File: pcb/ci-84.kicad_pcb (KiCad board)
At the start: 2 copper layers, 91 x 217 mm, 113 parts, among them J1 Conn_01x02, SW1 SW_Push, SW10 XT0N, SW11 STAT, SW12 MATH, SW13 APPS, SW14 PRGM, SW15 VARS, SW16 CLEAR, SW17 X^-1, SW18 SIN, SW19 COS, SW2 Y=, SW20 TAN, SW21 ^, SW22 X^2, SW23 ,, SW24 (, SW25 ), SW26 DIVIDE, SW27 LOG, SW28 7, SW29 8, SW3 WINDOW, SW30 9, SW31 MULITPLY, SW32 IN, SW33 4, SW34 5, SW35 6, SW36 SUBTRACT, SW37 STO, SW38 1, SW39 2, SW4 ZOOM, SW40 3, SW41 ADD, SW42 ON, SW43 0, SW44 ., SW45 (-), SW46 ENTER, SW47 GRAPH, SW48 UP, SW49 RIGHT, SW5 TRACE, SW50 DOWN, SW51 LEFT, SW6 2ND, SW7 MODE, SW8 DEL, SW9 ALPHA, U1 STM32L471RGTx, U3 TPS63900, U4 TFT_320x240

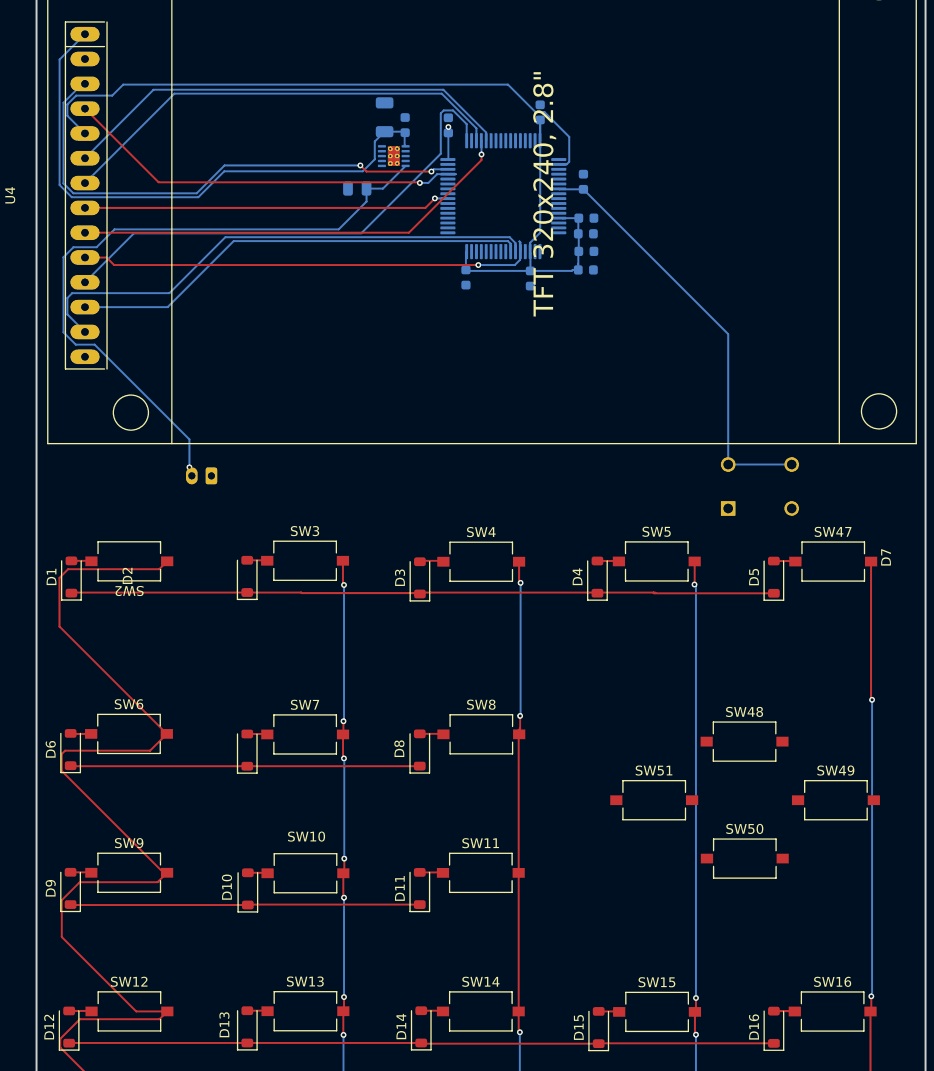
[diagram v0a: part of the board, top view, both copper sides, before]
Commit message: move arrow keys to keyboard matrix, add labels for riows
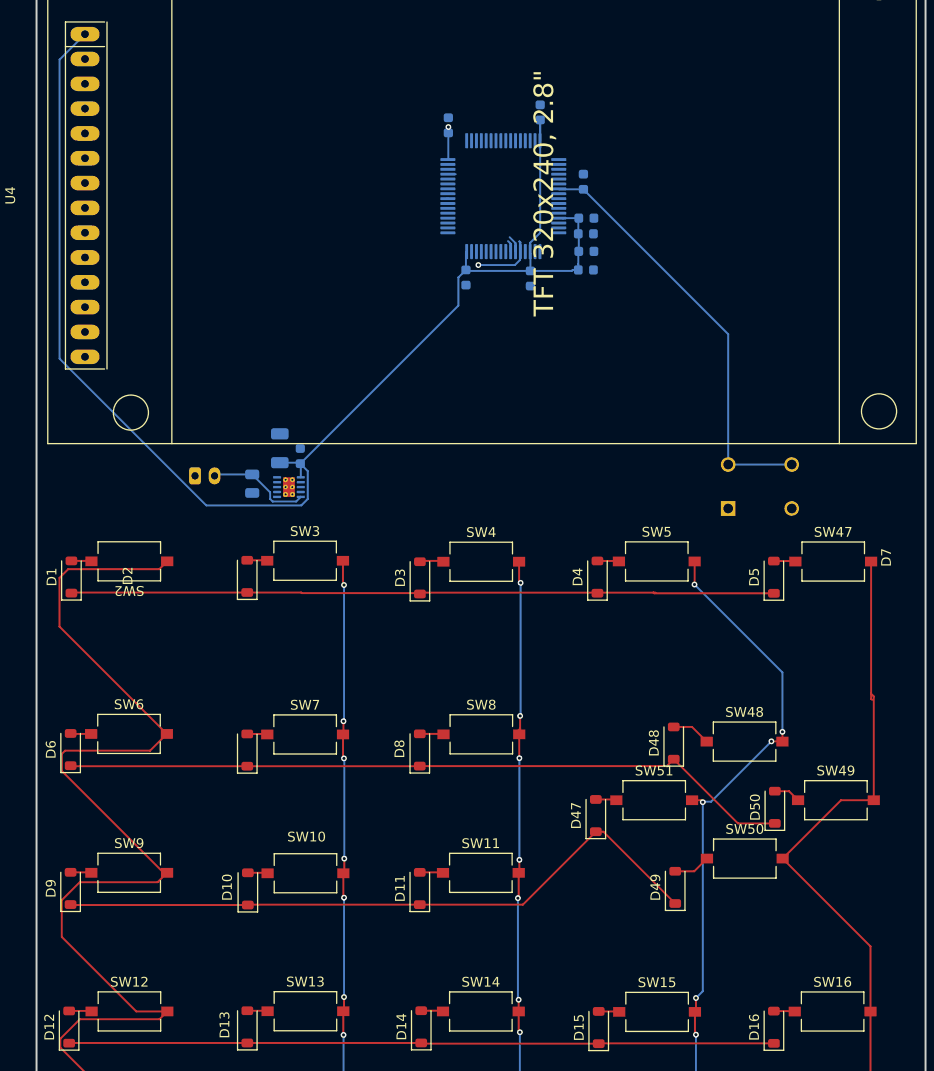
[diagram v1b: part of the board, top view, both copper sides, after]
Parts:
- added D47: D, Diode_SMD:D_SOD-123, F.Cu at (294.8, 182.7)
- added D48: D, Diode_SMD:D_SOD-123, F.Cu at (302.7, 175.2)
- added D49: D, Diode_SMD:D_SOD-123, F.Cu at (302.9, 190.0)
- added D50: D, Diode_SMD:D_SOD-123, F.Cu at (313.1, 181.8)
- moved U3 35.5 mm to (263.3, 149.1)
- moved C12 35.5 mm to (262.4, 145.1)
- moved C5 35.5 mm to (264.5, 145.9)
- moved C11 32.1 mm to (259.6, 148.7), turned to 90 degrees
- moved J1 1.68 mm to (253.7, 147.9), turned to 0 degrees
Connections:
- net Net-(D1-K) renamed /r1
- net Net-(D10-K) renamed /r3
- net Net-(D12-K) renamed /r4
- net Net-(D17-K) renamed /r5
- net Net-(D22-K) renamed /r6
- net Net-(D27-K) renamed /r7
- net Net-(D32-K) renamed /r8
- net Net-(D37-K) renamed /r9
- net Net-(D42-K) renamed /r10
- net Net-(D6-K) renamed /r2
- net Net-(SW10-Pad2) renamed /c2
- net Net-(SW11-Pad2) renamed /c3
- net Net-(SW12-Pad2) renamed /c1
- SW15 pad 2: Net-(SW15-Pad2) -> /c4
- SW16 pad 2: Net-(SW16-Pad2) -> /c5
- SW20 pad 2: Net-(SW15-Pad2) -> /c4
- SW21 pad 2: Net-(SW16-Pad2) -> /c5
- SW25 pad 2: Net-(SW15-Pad2) -> /c4
- SW26 pad 2: Net-(SW16-Pad2) -> /c5
- SW30 pad 2: Net-(SW15-Pad2) -> /c4
- SW31 pad 2: Net-(SW16-Pad2) -> /c5
- SW35 pad 2: Net-(SW15-Pad2) -> /c4
- SW36 pad 2: Net-(SW16-Pad2) -> /c5
- SW40 pad 2: Net-(SW15-Pad2) -> /c4
- SW41 pad 2: Net-(SW16-Pad2) -> /c5
- SW45 pad 2: Net-(SW15-Pad2) -> /c4
- SW46 pad 2: Net-(SW16-Pad2) -> /c5
- SW47 pad 2: Net-(SW16-Pad2) -> /c5
- SW48 pad 1: unconnected-(SW48-Pad1) -> Net-(D48-A)
- SW48 pad 2: unconnected-(SW48-Pad2) -> /c4
- SW49 pad 1: unconnected-(SW49-Pad1) -> Net-(D50-A)
- SW49 pad 2: unconnected-(SW49-Pad2) -> /c5
- SW5 pad 2: Net-(SW15-Pad2) -> /c4
- SW50 pad 1: unconnected-(SW50-Pad1) -> Net-(D49-A)
- SW50 pad 2: unconnected-(SW50-Pad2) -> /c5
- SW51 pad 1: unconnected-(SW51-Pad1) -> Net-(D47-A)
- SW51 pad 2: unconnected-(SW51-Pad2) -> /c4
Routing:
- net /c4: track 0.00 -> 152.5 mm, vias 0 -> 17
- net Net-(SW15-Pad2): track 142.9 -> 0.00 mm, vias 14 -> 0
- net /c5: track 0.00 -> 141.9 mm
- net Net-(SW16-Pad2): track 131.6 -> 0.00 mm, vias 2 -> 0
- net /IO_DC: track 61.9 -> 0.00 mm
- net +BATT: track 67.8 -> 10.6 mm, vias 1 -> 0
- net /SPI_CS: track 53.0 -> 0.66 mm, vias 2 -> 0
- net /TS_MISO: track 53.8 -> 1.72 mm
- net /TS_CS: track 51.1 -> 0.00 mm
- net /SPI3_MOSI: track 46.6 -> 0.00 mm
- net /SPI3_SCK: track 46.6 -> 0.00 mm
- net /TS_MOSI: track 47.3 -> 1.19 mm
- net /SPI_MISO: track 45.7 -> 0.03 mm, vias 1 -> 0
- net VDD: track 99.4 -> 142.1 mm
- net /SCREEN_RST: track 42.3 -> 0.81 mm, vias 1 -> 0
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
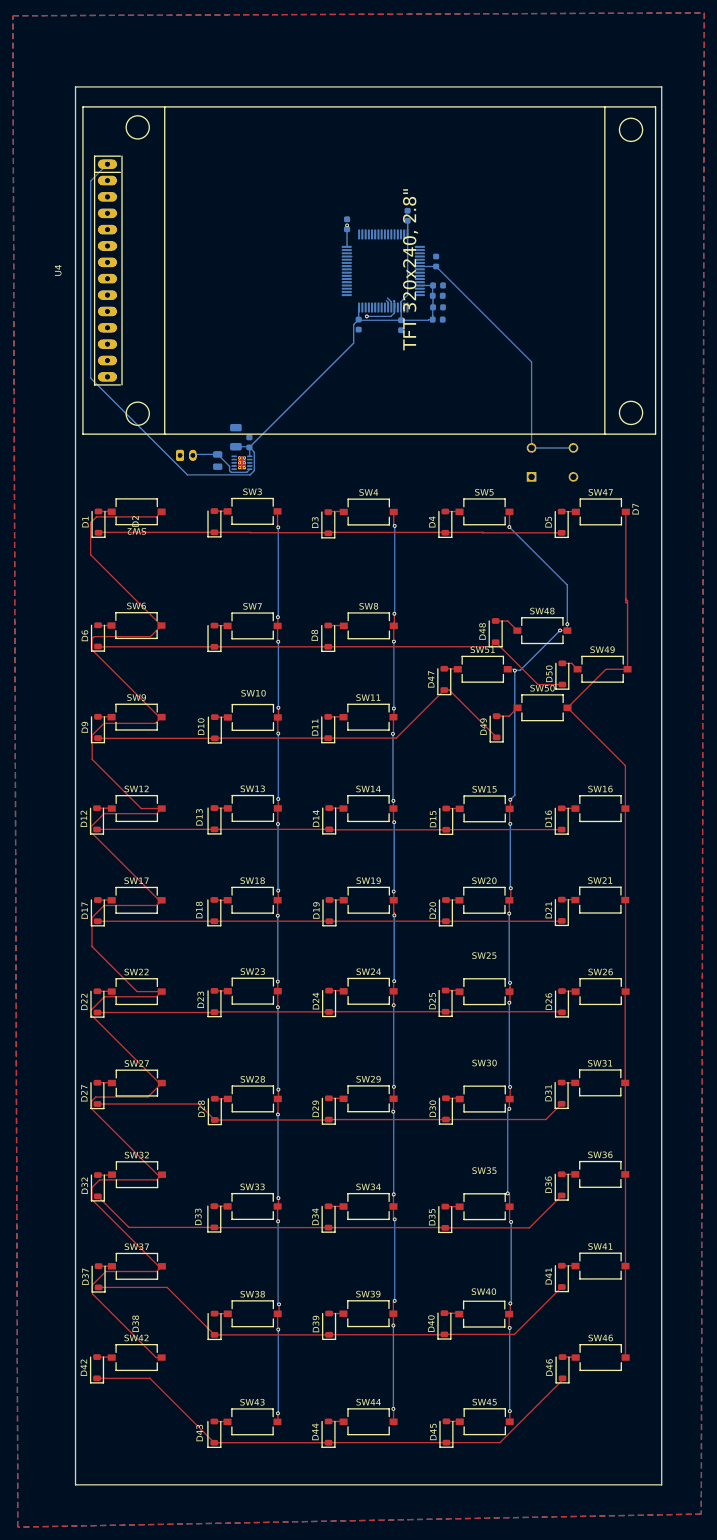
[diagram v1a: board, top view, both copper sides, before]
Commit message: finish matrix connections
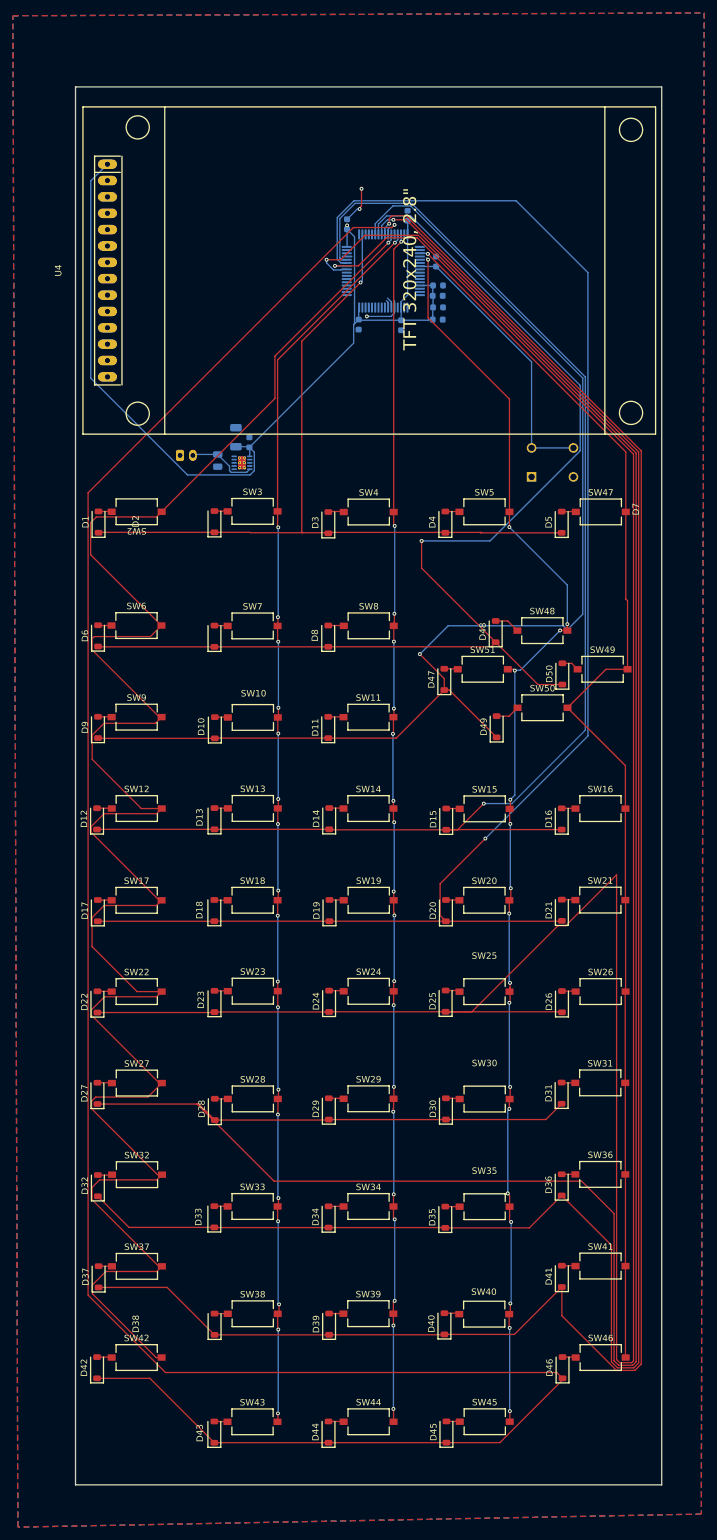
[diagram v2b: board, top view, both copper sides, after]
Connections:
- U1 pad 3: unconnected-(U1-PC14-Pad3) -> /c5
- U1 pad 4: unconnected-(U1-PC15-Pad4) -> /c4
- U1 pad 41: unconnected-(U1-PA8-Pad41) -> /r7
- U1 pad 42: unconnected-(U1-PA9-Pad42) -> /r6
- U1 pad 43: unconnected-(U1-PA10-Pad43) -> /r5
- U1 pad 44: unconnected-(U1-PA11-Pad44) -> /r4
- U1 pad 50: unconnected-(U1-PA15-Pad50) -> /r1
- U1 pad 54: unconnected-(U1-PD2-Pad54) -> /r3
- U1 pad 55: unconnected-(U1-PB3-Pad55) -> /r2
- U1 pad 56: unconnected-(U1-PB4-Pad56) -> /r8
- U1 pad 57: unconnected-(U1-PB5-Pad57) -> /r9
- U1 pad 58: unconnected-(U1-PB6-Pad58) -> /r10
- U1 pad 59: unconnected-(U1-PB7-Pad59) -> /c1
- U1 pad 61: unconnected-(U1-PB8-Pad61) -> /c2
- U1 pad 62: unconnected-(U1-PB9-Pad62) -> /c3
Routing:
- net /r6: track 72.2 -> 390.4 mm, vias 0 -> 1
- net /r7: track 74.1 -> 381.5 mm, vias 0 -> 1
- net /r10: track 80.7 -> 351.2 mm, vias 0 -> 1
- net /r8: track 76.1 -> 308.0 mm, vias 0 -> 1
- net /r9: track 78.0 -> 297.7 mm, vias 0 -> 1
- net /r5: track 72.1 -> 235.4 mm, vias 0 -> 1
- net /r4: track 72.2 -> 212.7 mm, vias 0 -> 1
- net /r3: track 68.1 -> 186.1 mm, vias 0 -> 1
- net /r2: track 75.2 -> 180.8 mm, vias 0 -> 1
- net /c1: track 262.4 -> 320.2 mm, vias 0 -> 1
- net /c5: track 141.9 -> 195.3 mm, vias 0 -> 1
- net /c2: track 142.2 -> 192.9 mm, vias 18 -> 19
- net /r1: track 72.2 -> 122.6 mm, vias 0 -> 1
- net /c4: track 152.5 -> 197.3 mm, vias 17 -> 18
- net /c3: track 142.3 -> 185.9 mm, vias 18 -> 19
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
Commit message: finish wiring everthing
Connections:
- U1 pad 2: /IO_DC -> unconnected-(U1-PC13-Pad2)
- U1 pad 21: /TS_CK -> unconnected-(U1-PA5-Pad21)
- U1 pad 22: /TS_MISO -> unconnected-(U1-PA6-Pad22)
- U1 pad 23: /TS_MOSI -> unconnected-(U1-PA7-Pad23)
- U1 pad 33: unconnected-(U1-PB12-Pad33) -> /TS_MISO
- U1 pad 34: unconnected-(U1-PB13-Pad34) -> /TS_MOSI
- U1 pad 35: unconnected-(U1-PB14-Pad35) -> /TS_CS
- U1 pad 36: unconnected-(U1-PB15-Pad36) -> /TS_CK
- U1 pad 37: unconnected-(U1-PC6-Pad37) -> /IO_LED
- U1 pad 38: unconnected-(U1-PC7-Pad38) -> /SPI3_SCK
- U1 pad 39: unconnected-(U1-PC8-Pad39) -> /SCREEN_RST
- U1 pad 40: /IO_LED -> /SPI_CS
- U1 pad 45: /SCREEN_RST -> unconnected-(U1-PA12-Pad45)
- U1 pad 46: /SPI_CS -> unconnected-(U1-PA13-Pad46)
- U1 pad 49: /TS_CS -> /IO_DC
- U1 pad 51: /SPI3_SCK -> unconnected-(U1-PC10-Pad51)
- U1 pad 52: /SPI_MISO -> /SPI3_MOSI
- U1 pad 53: /SPI3_MOSI -> /SPI_MISO
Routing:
- net /SPI_MISO: track 0.03 -> 65.7 mm, vias 0 -> 1
- net /SPI3_MOSI: track 0.00 -> 50.9 mm, vias 0 -> 1
- net /IO_DC: track 0.00 -> 42.3 mm, vias 0 -> 1
- net /SPI_CS: track 0.66 -> 42.7 mm
- net /SCREEN_RST: track 0.81 -> 41.2 mm
- net /TS_CS: track 0.00 -> 39.7 mm
- net /TS_MISO: track 1.72 -> 41.3 mm
- net /TS_MOSI: track 1.19 -> 40.5 mm
- net /SPI3_SCK: track 0.00 -> 38.3 mm
- net /IO_LED: track 0.03 -> 38.0 mm
- net /TS_CK: track 7.47 -> 38.8 mm, vias 1 -> 0
- net GND: track 5.88 -> 24.4 mm, vias 2 -> 5
- net /c4: track 197.3 -> 198.4 mm
- net unconnected-(U1-PA12-Pad45): track 0.00 -> 0.81 mm
- net VDD: vias 1 -> 0

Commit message: sheets for schematic
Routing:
- net GND: track 24.4 -> 37.0 mm, vias 5 -> 8
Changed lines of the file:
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@@
 			(outputformat 1)
 			(mirror no)
-			(drillshape 1)
+			(drillshape 0)
 			(scaleselection 1)
-			(outputdirectory "")
+			(outputdirectory "../../../Downloads/")
 		)
 	)
@@
 	)
 	(segment
+		(start 255.85 149.75)
+		(end 254.275 151.325)
+		(width 0.2)
+		(layer "F.Cu")
+		(net 2)
+	)
+	(segment
 		(start 281.6 109.65)
 		(end 281.6 109.45)
@@
 	)
 	(segment
+		(start 281.45 123.65)
+		(end 278.625 126.475)
+		(width 0.2)
+		(layer "F.Cu")
+		(net 2)
+	)
+	(segment
 		(start 281.673527 115.35)
 		(end 283.35 115.35)
@@
 	)
 	(segment
+		(start 254.275 151.325)
+		(end 253.25 151.325)
+		(width 0.2)
+		(layer "F.Cu")
+		(net 2)
+	)
+	(segment
 		(start 281.6 109.45)
 		(end 281.9 109.15)
@@
 	)
 	(via
+		(at 278.625 126.475)
+		(size 0.6)
+		(drill 0.3)
+		(layers "F.Cu" "B.Cu")
+		(net 2)
+	)
+	(via
 		(at 283.35 115.35)
 		(size 0.6)
@@
 		(net 2)
 	)
+	(via
+		(at 281.45 123.65)
+		(size 0.6)
+		(drill 0.3)
+		(layers "F.Cu" "B.Cu")
+		(net 2)
+	)
+	(via
+		(at 255.85 149.75)
+		(size 0.6)
+		(drill 0.3)
+		(layers "F.Cu" "B.Cu")
+		(net 2)
+	)
 	(segment
 		(start 288.53 124.945)
@@
 	)
 	(segment
+		(start 259.575 149.65)
+		(end 255.95 149.65)
+		(width 0.2)
+		(layer "B.Cu")
+		(net 2)
+	)
+	(segment
 		(start 262.9875 149.8)
 		(end 263.6875 149.8)
@@
 	)
 	(segment
+		(start 282.03 124.13759)
+		(end 281.54241 123.65)
+		(width 0.2)
+		(layer "B.Cu")
+		(net 2)
+	)
+	(segment
 		(start 262.9875 149.05)
 		(end 263.6875 149.05)
@@
 	)
 	(segment
+		(start 281.54241 123.65)
+		(end 281.45 123.65)
+		(width 0.2)
+		(layer "B.Cu")
+		(net 2)
+	)
+	(segment
 		(start 289.055 109.92)
 		(end 287.695 109.92)
@@
 	)
 	(segment
+		(start 282.03 124.945)
+		(end 282.03 124.13759)
+		(width 0.2)
+		(layer "B.Cu")
+		(net 2)
+	)
+	(segment
 		(start 262.9875 148.3)
 		(end 263.6875 148.3)
@@
 		(width 0.2)
 		(layer "B.Cu")
+		(net 2)
+	)
+	(segment
+		(start 255.95 149.65)
+		(end 255.85 149.75)
+		(width 0.2)
+		(layer "B.Cu")
